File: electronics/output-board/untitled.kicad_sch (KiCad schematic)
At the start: 5 parts, among them J2 Conn_01x02_Male

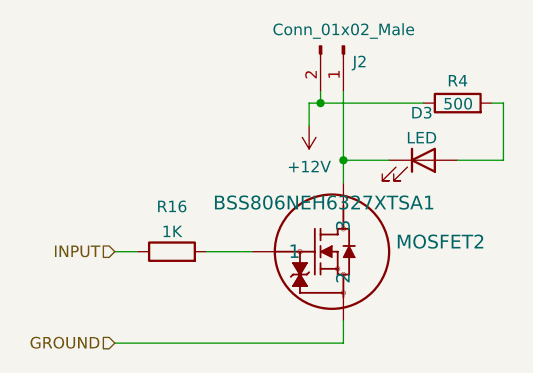
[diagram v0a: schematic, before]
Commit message: Working on ouput board.
Saving before using the replicate layout plugin.
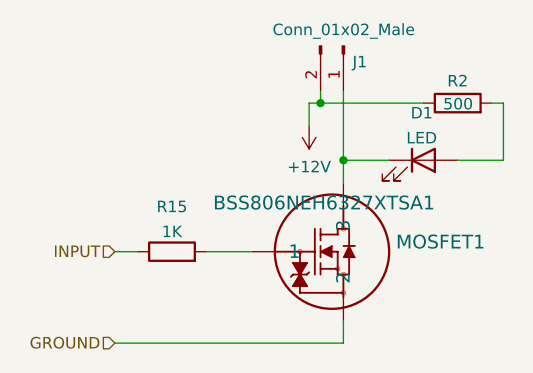
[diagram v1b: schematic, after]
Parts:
- renumbered D3 to D1, J2 to J1, MOSFET2 to MOSFET1, R16 to R15, R4 to R2
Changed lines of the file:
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@@
   (symbol (lib_id "power:+12V") (at 45.72 33.02 180)
     (in_bom yes) (on_board yes) (fields_autoplaced)
-    (property "Reference" "#PWR0144" (id 0) (at 45.72 29.21 0)
+    (property "Reference" "#PWR0133" (id 0) (at 45.72 29.21 0)
       (effects (font (size 1.27 1.27)) hide)
     )
@@
   (symbol (lib_id "Connector:Conn_01x02_Male") (at 49.53 24.13 270)
     (in_bom yes) (on_board yes)
-    (property "Reference" "J2" (id 0) (at 50.5461 25.9139 90)
+    (property "Reference" "J1" (id 0) (at 50.5461 25.9139 90)
       (effects (font (size 1.27 1.27)) (justify left))
     )
@@
   (symbol (lib_id "Device:R") (at 30.48 46.99 90)
     (in_bom yes) (on_board yes) (fields_autoplaced)
-    (property "Reference" "R16" (id 0) (at 30.48 42.0074 90))
+    (property "Reference" "R15" (id 0) (at 30.48 42.0074 90))
     (property "Value" "1K" (id 1) (at 30.48 44.7825 90))
     (property "Footprint" "Resistor_SMD:R_0603_1608Metric" (id 2) (at 30.48 48.768 90)
@@
   (symbol (lib_id "Device:R") (at 62.23 30.48 90)
     (in_bom yes) (on_board yes)
-    (property "Reference" "R4" (id 0) (at 62.23 28.0374 90))
+    (property "Reference" "R2" (id 0) (at 62.23 28.0374 90))
     (property "Value" "500" (id 1) (at 62.2775 30.5919 90))
     (property "Footprint" "Resistor_SMD:R_0603_1608Metric" (id 2) (at 62.23 32.258 90)
@@
   (symbol (lib_id "Device:LED") (at 58.42 36.83 0)
     (in_bom yes) (on_board yes) (fields_autoplaced)
-    (property "Reference" "D3" (id 0) (at 58.2295 31.5934 0))
+    (property "Reference" "D1" (id 0) (at 58.2295 31.5934 0))
     (property "Value" "LED" (id 1) (at 58.2295 34.3685 0))
     (property "Footprint" "LED_SMD:LED_1206_3216Metric" (id 2) (at 58.42 36.83 0)
@@
   (symbol (lib_id "2021-09-18_15-04-13:BSS806NEH6327XTSA1") (at 39.37 46.99 0)
     (in_bom yes) (on_board yes)
-    (property "Reference" "MOSFET2" (id 0) (at 55.3721 45.9253 0)
+    (property "Reference" "MOSFET1" (id 0) (at 55.3721 45.9253 0)
       (effects (font (size 1.524 1.524)) (justify left))
     )

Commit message: Output Board is basically done!
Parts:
- J1: footprint Connector_Molex:Molex_SL_171971-0002_1x02_P2.54mm_Vertical -> Connector_PinHeader_2.54mm:PinHeader_1x02_P2.54mm_Horizontal
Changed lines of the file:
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@@
       (effects (font (size 1.27 1.27)) (justify left))
     )
-    (property "Footprint" "Connector_Molex:Molex_SL_171971-0002_1x02_P2.54mm_Vertical" (id 2) (at 49.53 24.13 0)
+    (property "Footprint" "Connector_PinHeader_2.54mm:PinHeader_1x02_P2.54mm_Horizontal" (id 2) (at 49.53 24.13 0)
       (effects (font (size 1.27 1.27)) hide)
     )

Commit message: Put in connectors and finalized layout of everything except MCU.
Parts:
- J1: footprint Connector_PinHeader_2.54mm:PinHeader_1x02_P2.54mm_Horizontal -> CustomFootprints:LatchingConnector2POS
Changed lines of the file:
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@@
   (symbol (lib_id "power:+12V") (at 45.72 33.02 180)
     (in_bom yes) (on_board yes) (fields_autoplaced)
-    (property "Reference" "#PWR0133" (id 0) (at 45.72 29.21 0)
+    (property "Reference" "#PWR0144" (id 0) (at 45.72 29.21 0)
       (effects (font (size 1.27 1.27)) hide)
     )
@@
       (effects (font (size 1.27 1.27)) (justify left))
     )
-    (property "Footprint" "Connector_PinHeader_2.54mm:PinHeader_1x02_P2.54mm_Horizontal" (id 2) (at 49.53 24.13 0)
+    (property "Footprint" "CustomFootprints:LatchingConnector2POS" (id 2) (at 49.53 24.13 0)
       (effects (font (size 1.27 1.27)) hide)
     )

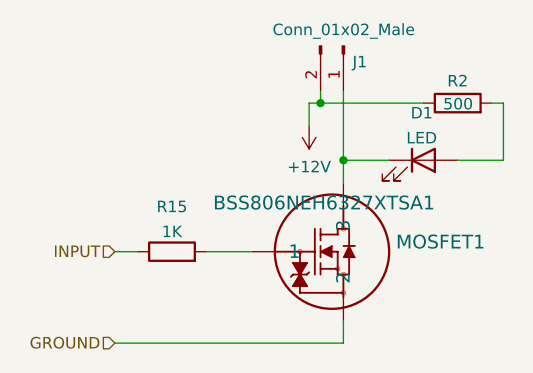
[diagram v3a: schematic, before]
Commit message: Updated MCU Base and started MCU on Output Board
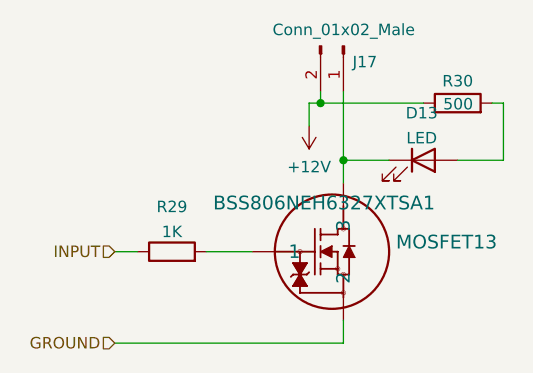
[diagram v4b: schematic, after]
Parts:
- renumbered D1 to D13, J1 to J17, MOSFET1 to MOSFET13, R15 to R29, R2 to R30
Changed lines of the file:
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@@
   (symbol (lib_id "Connector:Conn_01x02_Male") (at 49.53 24.13 270)
     (in_bom yes) (on_board yes)
-    (property "Reference" "J1" (id 0) (at 50.5461 25.9139 90)
+    (property "Reference" "J17" (id 0) (at 50.5461 25.9139 90)
       (effects (font (size 1.27 1.27)) (justify left))
     )
@@
   (symbol (lib_id "Device:R") (at 30.48 46.99 90)
     (in_bom yes) (on_board yes) (fields_autoplaced)
-    (property "Reference" "R15" (id 0) (at 30.48 42.0074 90))
+    (property "Reference" "R29" (id 0) (at 30.48 42.0074 90))
     (property "Value" "1K" (id 1) (at 30.48 44.7825 90))
     (property "Footprint" "Resistor_SMD:R_0603_1608Metric" (id 2) (at 30.48 48.768 90)
@@
   (symbol (lib_id "Device:R") (at 62.23 30.48 90)
     (in_bom yes) (on_board yes)
-    (property "Reference" "R2" (id 0) (at 62.23 28.0374 90))
+    (property "Reference" "R30" (id 0) (at 62.23 28.0374 90))
     (property "Value" "500" (id 1) (at 62.2775 30.5919 90))
     (property "Footprint" "Resistor_SMD:R_0603_1608Metric" (id 2) (at 62.23 32.258 90)
@@
   (symbol (lib_id "Device:LED") (at 58.42 36.83 0)
     (in_bom yes) (on_board yes) (fields_autoplaced)
-    (property "Reference" "D1" (id 0) (at 58.2295 31.5934 0))
+    (property "Reference" "D13" (id 0) (at 58.2295 31.5934 0))
     (property "Value" "LED" (id 1) (at 58.2295 34.3685 0))
     (property "Footprint" "LED_SMD:LED_1206_3216Metric" (id 2) (at 58.42 36.83 0)
@@
   (symbol (lib_id "2021-09-18_15-04-13:BSS806NEH6327XTSA1") (at 39.37 46.99 0)
     (in_bom yes) (on_board yes)
-    (property "Reference" "MOSFET1" (id 0) (at 55.3721 45.9253 0)
+    (property "Reference" "MOSFET13" (id 0) (at 55.3721 45.9253 0)
       (effects (font (size 1.524 1.524)) (justify left))
     )

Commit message: Continued Laying Out Output Board
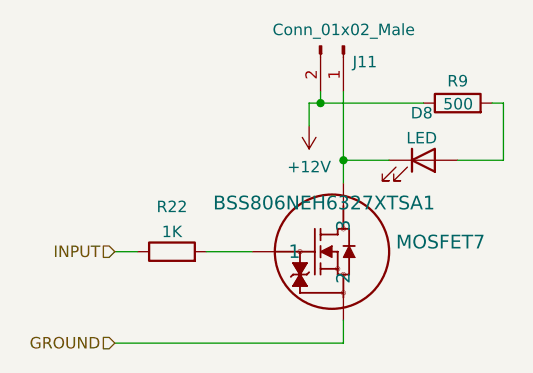
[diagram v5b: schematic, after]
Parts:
- renumbered D13 to D8, J17 to J11, MOSFET13 to MOSFET7, R29 to R22, R30 to R9
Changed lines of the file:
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@@
   (symbol (lib_id "Connector:Conn_01x02_Male") (at 49.53 24.13 270)
     (in_bom yes) (on_board yes)
-    (property "Reference" "J17" (id 0) (at 50.5461 25.9139 90)
+    (property "Reference" "J11" (id 0) (at 50.5461 25.9139 90)
       (effects (font (size 1.27 1.27)) (justify left))
     )
@@
   (symbol (lib_id "Device:R") (at 30.48 46.99 90)
     (in_bom yes) (on_board yes) (fields_autoplaced)
-    (property "Reference" "R29" (id 0) (at 30.48 42.0074 90))
+    (property "Reference" "R22" (id 0) (at 30.48 42.0074 90))
     (property "Value" "1K" (id 1) (at 30.48 44.7825 90))
     (property "Footprint" "Resistor_SMD:R_0603_1608Metric" (id 2) (at 30.48 48.768 90)
@@
   (symbol (lib_id "Device:R") (at 62.23 30.48 90)
     (in_bom yes) (on_board yes)
-    (property "Reference" "R30" (id 0) (at 62.23 28.0374 90))
+    (property "Reference" "R9" (id 0) (at 62.23 28.0374 90))
     (property "Value" "500" (id 1) (at 62.2775 30.5919 90))
     (property "Footprint" "Resistor_SMD:R_0603_1608Metric" (id 2) (at 62.23 32.258 90)
@@
   (symbol (lib_id "Device:LED") (at 58.42 36.83 0)
     (in_bom yes) (on_board yes) (fields_autoplaced)
-    (property "Reference" "D13" (id 0) (at 58.2295 31.5934 0))
+    (property "Reference" "D8" (id 0) (at 58.2295 31.5934 0))
     (property "Value" "LED" (id 1) (at 58.2295 34.3685 0))
     (property "Footprint" "LED_SMD:LED_1206_3216Metric" (id 2) (at 58.42 36.83 0)
@@
   (symbol (lib_id "2021-09-18_15-04-13:BSS806NEH6327XTSA1") (at 39.37 46.99 0)
     (in_bom yes) (on_board yes)
-    (property "Reference" "MOSFET13" (id 0) (at 55.3721 45.9253 0)
+    (property "Reference" "MOSFET7" (id 0) (at 55.3721 45.9253 0)
       (effects (font (size 1.524 1.524)) (justify left))
     )

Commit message: continued working on four-layer output board
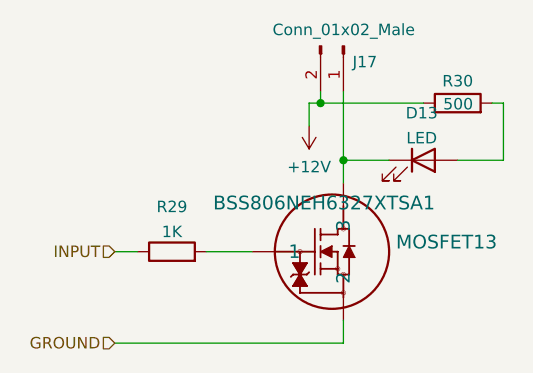
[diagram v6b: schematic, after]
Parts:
- renumbered D8 to D13, J11 to J17, MOSFET7 to MOSFET13, R22 to R29, R9 to R30
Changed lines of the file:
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@@
   (symbol (lib_id "Connector:Conn_01x02_Male") (at 49.53 24.13 270)
     (in_bom yes) (on_board yes)
-    (property "Reference" "J11" (id 0) (at 50.5461 25.9139 90)
+    (property "Reference" "J17" (id 0) (at 50.5461 25.9139 90)
       (effects (font (size 1.27 1.27)) (justify left))
     )
@@
   (symbol (lib_id "Device:R") (at 30.48 46.99 90)
     (in_bom yes) (on_board yes) (fields_autoplaced)
-    (property "Reference" "R22" (id 0) (at 30.48 42.0074 90))
+    (property "Reference" "R29" (id 0) (at 30.48 42.0074 90))
     (property "Value" "1K" (id 1) (at 30.48 44.7825 90))
     (property "Footprint" "Resistor_SMD:R_0603_1608Metric" (id 2) (at 30.48 48.768 90)
@@
   (symbol (lib_id "Device:R") (at 62.23 30.48 90)
     (in_bom yes) (on_board yes)
-    (property "Reference" "R9" (id 0) (at 62.23 28.0374 90))
+    (property "Reference" "R30" (id 0) (at 62.23 28.0374 90))
     (property "Value" "500" (id 1) (at 62.2775 30.5919 90))
     (property "Footprint" "Resistor_SMD:R_0603_1608Metric" (id 2) (at 62.23 32.258 90)
@@
   (symbol (lib_id "Device:LED") (at 58.42 36.83 0)
     (in_bom yes) (on_board yes) (fields_autoplaced)
-    (property "Reference" "D8" (id 0) (at 58.2295 31.5934 0))
+    (property "Reference" "D13" (id 0) (at 58.2295 31.5934 0))
     (property "Value" "LED" (id 1) (at 58.2295 34.3685 0))
     (property "Footprint" "LED_SMD:LED_1206_3216Metric" (id 2) (at 58.42 36.83 0)
@@
   (symbol (lib_id "2021-09-18_15-04-13:BSS806NEH6327XTSA1") (at 39.37 46.99 0)
     (in_bom yes) (on_board yes)
-    (property "Reference" "MOSFET7" (id 0) (at 55.3721 45.9253 0)
+    (property "Reference" "MOSFET13" (id 0) (at 55.3721 45.9253 0)
       (effects (font (size 1.524 1.524)) (justify left))
     )

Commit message: added power leds and ignition detection
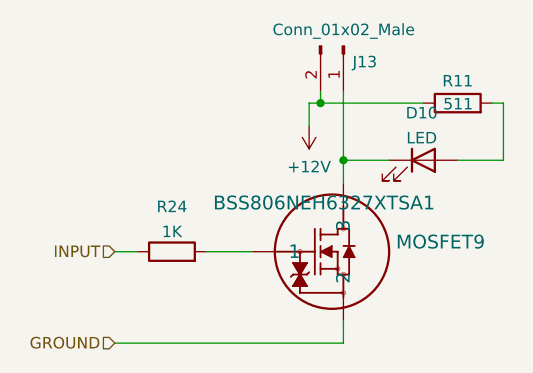
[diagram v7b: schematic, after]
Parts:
- R11: renamed from R30; value 500 -> 511
- renumbered D13 to D10, J17 to J13, MOSFET13 to MOSFET9, R29 to R24
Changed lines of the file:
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@@
   (symbol (lib_id "power:+12V") (at 45.72 33.02 180)
     (in_bom yes) (on_board yes) (fields_autoplaced)
-    (property "Reference" "#PWR0144" (id 0) (at 45.72 29.21 0)
+    (property "Reference" "#PWR0141" (id 0) (at 45.72 29.21 0)
       (effects (font (size 1.27 1.27)) hide)
     )
@@
   (symbol (lib_id "Connector:Conn_01x02_Male") (at 49.53 24.13 270)
     (in_bom yes) (on_board yes)
-    (property "Reference" "J17" (id 0) (at 50.5461 25.9139 90)
+    (property "Reference" "J13" (id 0) (at 50.5461 25.9139 90)
       (effects (font (size 1.27 1.27)) (justify left))
     )
@@
   (symbol (lib_id "Device:R") (at 30.48 46.99 90)
     (in_bom yes) (on_board yes) (fields_autoplaced)
-    (property "Reference" "R29" (id 0) (at 30.48 42.0074 90))
+    (property "Reference" "R24" (id 0) (at 30.48 42.0074 90))
     (property "Value" "1K" (id 1) (at 30.48 44.7825 90))
     (property "Footprint" "Resistor_SMD:R_0603_1608Metric" (id 2) (at 30.48 48.768 90)
@@
   (symbol (lib_id "Device:R") (at 62.23 30.48 90)
     (in_bom yes) (on_board yes)
-    (property "Reference" "R30" (id 0) (at 62.23 28.0374 90))
-    (property "Value" "500" (id 1) (at 62.2775 30.5919 90))
+    (property "Reference" "R11" (id 0) (at 62.23 28.0374 90))
+    (property "Value" "511" (id 1) (at 62.2775 30.5919 90))
     (property "Footprint" "Resistor_SMD:R_0603_1608Metric" (id 2) (at 62.23 32.258 90)
       (effects (font (size 1.27 1.27)) hide)
@@
   (symbol (lib_id "Device:LED") (at 58.42 36.83 0)
     (in_bom yes) (on_board yes) (fields_autoplaced)
-    (property "Reference" "D13" (id 0) (at 58.2295 31.5934 0))
+    (property "Reference" "D10" (id 0) (at 58.2295 31.5934 0))
     (property "Value" "LED" (id 1) (at 58.2295 34.3685 0))
     (property "Footprint" "LED_SMD:LED_1206_3216Metric" (id 2) (at 58.42 36.83 0)
@@
   (symbol (lib_id "2021-09-18_15-04-13:BSS806NEH6327XTSA1") (at 39.37 46.99 0)
     (in_bom yes) (on_board yes)
-    (property "Reference" "MOSFET13" (id 0) (at 55.3721 45.9253 0)
+    (property "Reference" "MOSFET9" (id 0) (at 55.3721 45.9253 0)
       (effects (font (size 1.524 1.524)) (justify left))
     )

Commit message: Added test cases for output board
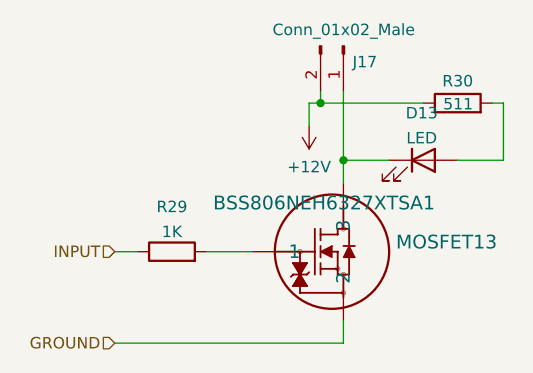
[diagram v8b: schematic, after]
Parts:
- renumbered D10 to D13, J13 to J17, MOSFET9 to MOSFET13, R24 to R29, R11 to R30
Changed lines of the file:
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@@
-(kicad_sch (version 20210621) (generator eeschema)
+(kicad_sch (version 20211123) (generator eeschema)
   (paper "A4")
-  (junction (at 46.99 30.48) (diameter 0) (color 0 0 0 0))
-  (junction (at 49.53 36.83) (diameter 0) (color 0 0 0 0))
-  (wire (pts (xy 24.13 46.99) (xy 26.67 46.99))
+  (junction (at 49.53 36.83) (diameter 0) (color 0 0 0 0)
+  )
+  (junction (at 46.99 30.48) (diameter 0) (color 0 0 0 0)
+  )
+  (wire (pts (xy 62.23 36.83) (xy 67.31 36.83))
+    (stroke (width 0) (type default) (color 0 0 0 0))
+  )
+  (wire (pts (xy 46.99 30.48) (xy 58.42 30.48))
+    (stroke (width 0) (type default) (color 0 0 0 0))
+  )
+  (wire (pts (xy 49.53 54.61) (xy 49.53 57.15))
+    (stroke (width 0) (type default) (color 0 0 0 0))
+  )
+  (wire (pts (xy 49.53 36.83) (xy 54.61 36.83))
+    (stroke (width 0) (type default) (color 0 0 0 0))
+  )
+  (wire (pts (xy 66.04 30.48) (xy 67.31 30.48))
+    (stroke (width 0) (type default) (color 0 0 0 0))
+  )
+  (wire (pts (xy 67.31 30.48) (xy 67.31 36.83))
     (stroke (width 0) (type default) (color 0 0 0 0))
   )
@@
     (stroke (width 0) (type default) (color 0 0 0 0))
   )
+  (wire (pts (xy 49.53 29.21) (xy 49.53 36.83))
+    (stroke (width 0) (type default) (color 0 0 0 0))
+  )
+  (wire (pts (xy 49.53 36.83) (xy 49.53 39.37))
+    (stroke (width 0) (type default) (color 0 0 0 0))
+  )
   (wire (pts (xy 34.29 46.99) (xy 39.37 46.99))
+    (stroke (width 0) (type default) (color 0 0 0 0))
+  )
+  (wire (pts (xy 24.13 46.99) (xy 26.67 46.99))
+    (stroke (width 0) (type default) (color 0 0 0 0))
+  )
+  (wire (pts (xy 46.99 29.21) (xy 46.99 30.48))
     (stroke (width 0) (type default) (color 0 0 0 0))
   )
@@
     (stroke (width 0) (type default) (color 0 0 0 0))
   )
-  (wire (pts (xy 46.99 29.21) (xy 46.99 30.48))
-    (stroke (width 0) (type default) (color 0 0 0 0))
-  )
-  (wire (pts (xy 46.99 30.48) (xy 58.42 30.48))
-    (stroke (width 0) (type default) (color 0 0 0 0))
-  )
-  (wire (pts (xy 49.53 29.21) (xy 49.53 36.83))
-    (stroke (width 0) (type default) (color 0 0 0 0))
-  )
-  (wire (pts (xy 49.53 36.83) (xy 49.53 39.37))
-    (stroke (width 0) (type default) (color 0 0 0 0))
-  )
-  (wire (pts (xy 49.53 36.83) (xy 54.61 36.83))
-    (stroke (width 0) (type default) (color 0 0 0 0))
-  )
-  (wire (pts (xy 49.53 54.61) (xy 49.53 57.15))
-    (stroke (width 0) (type default) (color 0 0 0 0))
-  )
-  (wire (pts (xy 62.23 36.83) (xy 67.31 36.83))
-    (stroke (width 0) (type default) (color 0 0 0 0))
-  )
-  (wire (pts (xy 66.04 30.48) (xy 67.31 30.48))
-    (stroke (width 0) (type default) (color 0 0 0 0))
-  )
-  (wire (pts (xy 67.31 30.48) (xy 67.31 36.83))
-    (stroke (width 0) (type default) (color 0 0 0 0))
+  (hierarchical_label "GROUND" (shape input) (at 24.13 57.15 180)
+    (effects (font (size 1.27 1.27)) (justify right))
   )
   (hierarchical_label "INPUT" (shape input) (at 24.13 46.99 180)
     (effects (font (size 1.27 1.27)) (justify right))
   )
-  (hierarchical_label "GROUND" (shape input) (at 24.13 57.15 180)
-    (effects (font (size 1.27 1.27)) (justify right))
-  )
   (symbol (lib_id "power:+12V") (at 45.72 33.02 180)
     (in_bom yes) (on_board yes) (fields_autoplaced)
-    (property "Reference" "#PWR0141" (id 0) (at 45.72 29.21 0)
+    (property "Reference" "#PWR0144" (id 0) (at 45.72 29.21 0)
       (effects (font (size 1.27 1.27)) hide)
     )
@@
     (pin "1")
   )
+  (symbol (lib_id "2021-09-18_15-04-13:BSS806NEH6327XTSA1") (at 39.37 46.99 0)
+    (in_bom yes) (on_board yes)
+    (property "Reference" "MOSFET13" (id 0) (at 55.3721 45.9253 0)
+      (effects (font (size 1.524 1.524)) (justify left))
+    )
+    (property "Value" "BSS806NEH6327XTSA1" (id 1) (at 35.0521 41.5843 0)
+      (effects (font (size 1.524 1.524)) (justify left))
+    )
+    (property "Footprint" "MOSFET:BSS806NEH6327XTSA1" (id 2) (at 50.8 53.594 0)
+      (effects (font (size 1.524 1.524)) hide)
+    )
+    (property "Datasheet" "" (id 3) (at 39.37 46.99 0)
+      (effects (font (size 1.524 1.524)))
+    )
+    (pin "1")
+    (pin "2")
+    (pin "3")
+  )
   (symbol (lib_id "Connector:Conn_01x02_Male") (at 49.53 24.13 270)
     (in_bom yes) (on_board yes)
-    (property "Reference" "J13" (id 0) (at 50.5461 25.9139 90)
+    (property "Reference" "J17" (id 0) (at 50.5461 25.9139 90)
       (effects (font (size 1.27 1.27)) (justify left))
     )
@@
   (symbol (lib_id "Device:R") (at 30.48 46.99 90)
     (in_bom yes) (on_board yes) (fields_autoplaced)
-    (property "Reference" "R24" (id 0) (at 30.48 42.0074 90))
+    (property "Reference" "R29" (id 0) (at 30.48 42.0074 90))
     (property "Value" "1K" (id 1) (at 30.48 44.7825 90))
     (property "Footprint" "Resistor_SMD:R_0603_1608Metric" (id 2) (at 30.48 48.768 90)
@@
   (symbol (lib_id "Device:R") (at 62.23 30.48 90)
     (in_bom yes) (on_board yes)
-    (property "Reference" "R11" (id 0) (at 62.23 28.0374 90))
+    (property "Reference" "R30" (id 0) (at 62.23 28.0374 90))
     (property "Value" "511" (id 1) (at 62.2775 30.5919 90))
     (property "Footprint" "Resistor_SMD:R_0603_1608Metric" (id 2) (at 62.23 32.258 90)
@@
   (symbol (lib_id "Device:LED") (at 58.42 36.83 0)
     (in_bom yes) (on_board yes) (fields_autoplaced)
-    (property "Reference" "D10" (id 0) (at 58.2295 31.5934 0))
+    (property "Reference" "D13" (id 0) (at 58.2295 31.5934 0))
     (property "Value" "LED" (id 1) (at 58.2295 34.3685 0))
     (property "Footprint" "LED_SMD:LED_1206_3216Metric" (id 2) (at 58.42 36.83 0)
@@
     (pin "2")
   )
-  (symbol (lib_id "2021-09-18_15-04-13:BSS806NEH6327XTSA1") (at 39.37 46.99 0)
-    (in_bom yes) (on_board yes)
-    (property "Reference" "MOSFET9" (id 0) (at 55.3721 45.9253 0)
-      (effects (font (size 1.524 1.524)) (justify left))
-    )
-    (property "Value" "BSS806NEH6327XTSA1" (id 1) (at 35.0521 41.5843 0)
-      (effects (font (size 1.524 1.524)) (justify left))
-    )
-    (property "Footprint" "MOSFET:BSS806NEH6327XTSA1" (id 2) (at 50.8 53.594 0)
-      (effects (font (size 1.524 1.524)) hide)
-    )
-    (property "Datasheet" "" (id 3) (at 39.37 46.99 0)
-      (effects (font (size 1.524 1.524)))
-    )
-    (pin "1")
-    (pin "2")
-    (pin "3")
-  )
 )
